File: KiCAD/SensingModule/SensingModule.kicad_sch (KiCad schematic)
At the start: 14 parts, among them J1 BUS, J2 MONITOR, U1 Arduino MKR WAN 1310

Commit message: 配線をつなげようとしたがうまくいかず　もう少し考えてみる
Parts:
- added H1, H2, H3, H4: MountingHole, MountingHole:MountingHole_4.3mm_M4, symbol Mechanical:MountingHole
- J1, J2: footprint Hirose_Connector:Hirose_DF11B-8DP-2DS -> TSRP_Connector:DF11-8DP-2DS
- U1: footprint ARDUINO_MKR_WAN_1310:BOARD_ARDUINO_MKR_WAN_1310 -> ARDUINO_MKR_WAN_1310 (1):BOARD_ARDUINO_MKR_WAN_1310

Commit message: MKRWAN問題解決
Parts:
- removed U1: Arduino MKR WAN 1310, ARDUINO_MKR_WAN_1310 (1):BOARD_ARDUINO_MKR_WAN_1310, symbol ABX00012:ABX00012
- added U1: ARDUINO_MKR_WAN_1310, TSRP_Arduino:BOARD_ARDUINO_MKR_WAN_1310, symbol ARDUINO_MKR_WAN_1310:ARDUINO_MKR_WAN_1310
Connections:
- net +3.3V: now also U1.J5_12 (+3V3)
- net +5V: now also U1.J5_13 (VIN)
- net CAN_RECEIVE_STATUS: now also U1.J3_9 (PA22/D0(PWM))
- net CAN_SEND_STATUS: now also U1.J3_10 (PA23/D1(PWM))
- net GND: now also U1.J5_11 (GND)
- net I2C_SCK: now also R8.1, U1.J5_7 (PA09/D12(PWM)/SCL(SC2)); no longer R7.1
- net I2C_SDA: now also R7.1, U1.J5_6 (PA08/D11/SDA(SC2)); no longer R8.1
- net LORA_RECEIVE_STATUS: now also U1.J3_13 (PB10/D4(PWM))
- net LORA_SEND_STATUS: now also U1.J3_14 (PB11/D5(PWM))
- net SPI_CS_FRAM0: now also U1.J3_3 (PB02/D16/AIN(10)/A1)
- net SPI_CS_FRAM1: now also U1.J3_4 (PB03/D17/AIN(11)/A2)
- net SPI_CS_FRAM2: now also U1.J3_11 (PA10/D2(PWM))
- net SPI_CS_FRAM3: now also U1.J3_12 (PA11/D3(PWM))
- net SPI_CS_MCP: now also U1.J5_2 (PA21/D7(PWM))
- net SPI_MISO: now also U1.J5_5 (PA19/D10(PWM)/CIPO(SC1))
- net SPI_MOSI: now also U1.J5_3 (PA16/D8(PWM)/COPI(SC1))
- net SPI_SCLK: now also U1.J5_4 (PA17/D9/SCK(SC1))
- net VREF_T1: now also U1.J3_5 (PA04/D18(PWM)/AIN(4)/A3)
- net VREF_T2: now also U1.J3_6 (PA05/D19(PWM)/AIN(5)/A4)
- net VREF_T3: now also U1.J3_7 (PA06/D20/AIN(6)/A5)
- net VREF_T4: now also U1.J3_8 (PA07/D21/AIN(7)/A6)
- net VREF_THERMISTOR: now also U1.J3_2 (PA02/D15/DAC0/AIN(0)/A0)
- no-connect marks 5 -> 6
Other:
- moved on the sheet: R3, R4, R5, R6, R7, R8, R9

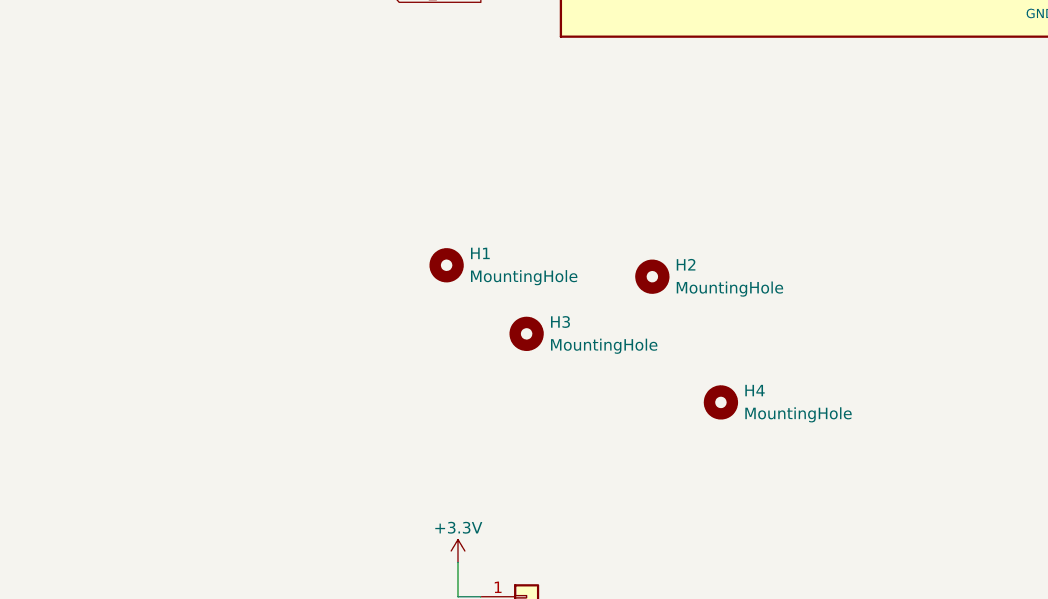
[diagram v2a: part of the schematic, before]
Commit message: 配線作業終了、確認お願いします
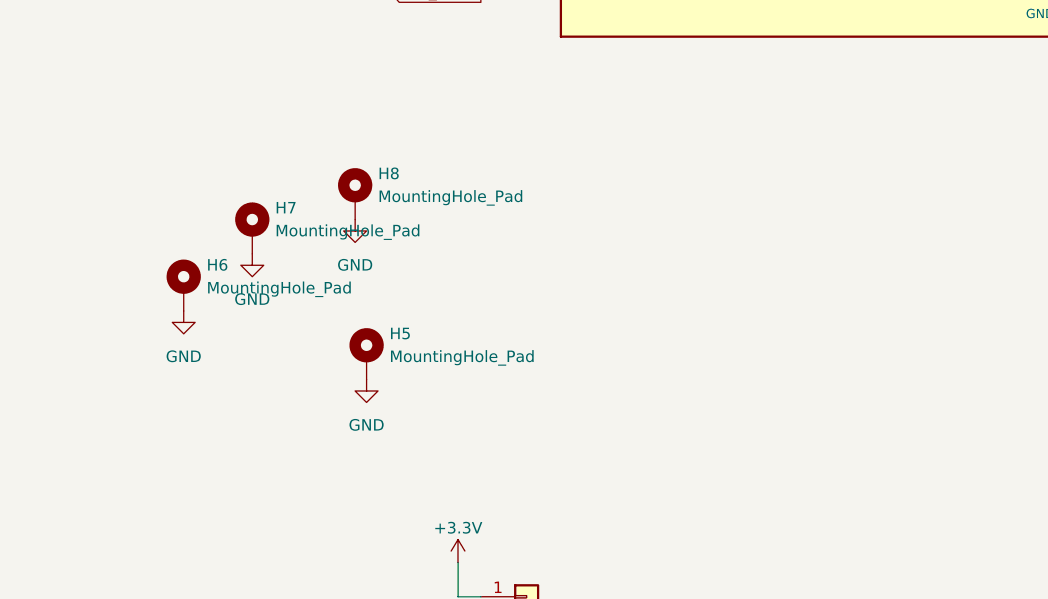
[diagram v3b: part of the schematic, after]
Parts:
- removed H1, H2, H3, H4: MountingHole, MountingHole:MountingHole_4.3mm_M4, symbol Mechanical:MountingHole
- added H5, H6, H7, H8: MountingHole_Pad, MountingHole:MountingHole_3.2mm_M3_DIN965_Pad_TopBottom, symbol Mechanical:MountingHole_Pad
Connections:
- net GND: now also H5.1, H6.1, H7.1, H8.1

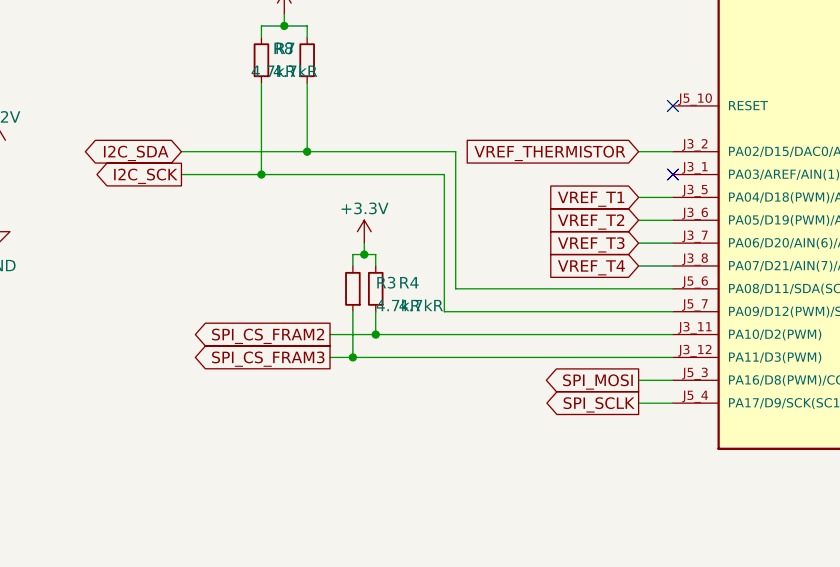
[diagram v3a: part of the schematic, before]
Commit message: Sensingの配線作業終わり、確認お願いします。
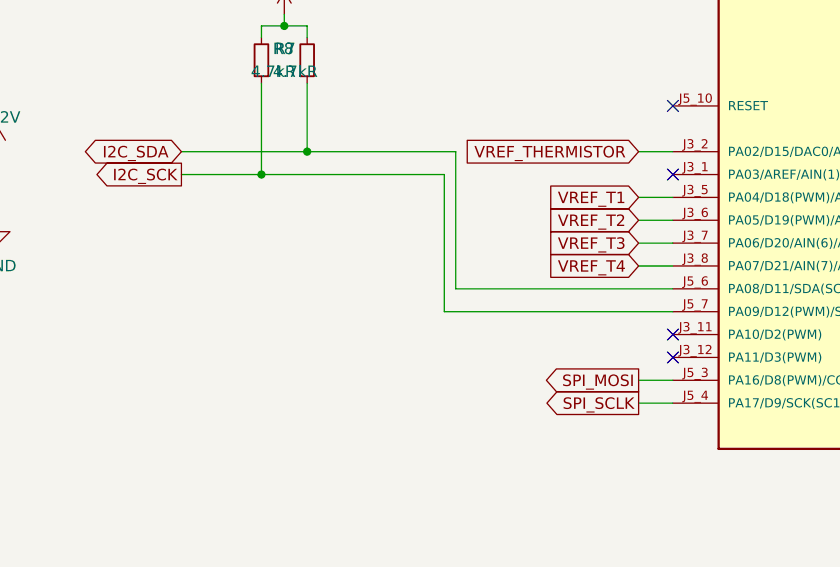
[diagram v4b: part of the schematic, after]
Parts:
- removed R3, R4: 4.7kR, Resistor_SMD:R_0603_1608Metric_Pad0.98x0.95mm_HandSolder, symbol Device:R_Small
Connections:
- net SPI_CS_FRAM2: no longer names the net of U1.J3_11 (PA10/D2(PWM))
- net SPI_CS_FRAM3: no longer names the net of U1.J3_12 (PA11/D3(PWM))
- no-connect marks 6 -> 8

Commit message: 配線確認お願いします
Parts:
- added R16: 4.7kR, Resistor_SMD:R_0603_1608Metric_Pad0.98x0.95mm_HandSolder, symbol Device:R_Small
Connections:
- net +3.3V: now also R16.2
- net SPI_CS_FRAM2: now reaches U1.J3_11 (PA10/D2(PWM))
- net SPI_CS_FRAM2: now also R16.1
- no-connect marks 8 -> 7
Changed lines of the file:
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@@
 	)
 	(junction
+		(at 102.87 73.66)
+		(diameter 0)
+		(color 0 0 0 0)
+	)
+	(junction
 		(at 255.27 53.34)
 		(diameter 0)
@@
 	)
 	(no_connect
-		(at 143.51 73.66)
-	)
-	(no_connect
 		(at 143.51 76.2)
 	)
@@
 	(wire
 		(pts
+			(xy 95.25 73.66) (xy 102.87 73.66)
+		)
+		(stroke
+			(width 0)
+			(type default)
+		)
+	)
+	(wire
+		(pts
 			(xy 63.5 130.81) (xy 63.5 133.35)
 		)
@@
 		)
 	)
+	(wire
+		(pts
+			(xy 102.87 69.85) (xy 102.87 73.66)
+		)
+		(stroke
+			(width 0)
+			(type default)
+		)
+	)
 	(bus
 		(pts
@@
 		)
 	)
+	(wire
+		(pts
+			(xy 102.87 73.66) (xy 143.51 73.66)
+		)
+		(stroke
+			(width 0)
+			(type default)
+		)
+	)
 	(label "GND"
 		(at 52.07 38.1 180)
@@
 		)
 	)
+	(global_label "SPI_CS_FRAM2"
+		(shape output)
+		(at 95.25 73.66 180)
+		(fields_autoplaced yes)
+		(effects
+			(font
+				(size 1.27 1.27)
+			)
+			(justify right)
+		)
+		(property "Intersheetrefs" "${INTERSHEET_REFS}"
+			(at 78.6577 73.66 0)
+			(effects
+				(font
+					(size 1.27 1.27)
+				)
+				(justify right)
+				(hide yes)
+			)
+		)
+	)
 	(global_label "VREF_THERMISTOR"
 		(shape input)
@@
 	)
 	(symbol
+		(lib_name "+3.3V_2")
+		(lib_id "power:+3.3V")
+		(at 102.87 64.77 0)
+		(unit 1)
+		(exclude_from_sim no)
+		(in_bom yes)
+		(on_board yes)
+		(dnp no)
+		(fields_autoplaced yes)
+		(property "Reference" "#PWR05"
+			(at 102.87 68.58 0)
+			(effects
+				(font
+					(size 1.27 1.27)
+				)
+				(hide yes)
+			)
+		)
+		(property "Value" "+3.3V"
+			(at 102.87 59.69 0)
+			(effects
+				(font
+					(size 1.27 1.27)
+				)
+			)
+		)
+		(property "Footprint" ""
+			(at 102.87 64.77 0)
+			(effects
+				(font
+					(size 1.27 1.27)
+				)
+				(hide yes)
+			)
+		)
+		(property "Datasheet" ""
+			(at 102.87 64.77 0)
+			(effects
+				(font
+					(size 1.27 1.27)
+				)
+				(hide yes)
+			)
+		)
+		(property "Description" "Power symbol creates a global label with name \"+3.3V\""
+			(at 102.87 64.77 0)
+			(effects
+				(font
+					(size 1.27 1.27)
+				)
+				(hide yes)
+			)
+		)
+		(pin "1"
+		)
+		(instances
+			(project ""
+				(path "/5f6205c9-e8e0-4a74-82d8-bdf647a68791"
+					(reference "#PWR05")
+					(unit 1)
+				)
+			)
+		)
+	)
+	(symbol
 		(lib_id "power:+3.3V")
 		(at 255.27 43.18 0)
@@
 					(unit 1)
 				)
+			)
+		)
+	)
+	(symbol
+		(lib_id "Device:R_Small")
+		(at 102.87 67.31 180)
+		(unit 1)
+		(exclude_from_sim no)
+		(in_bom yes)
+		(on_board yes)
+		(dnp no)
+		(property "Reference" "R16"
+			(at 104.14 66.04 0)
+			(effects
+				(font
+					(size 1.27 1.27)
+				)
+				(justify right)
+			)
+		)
+		(property "Value" "4.7kR"
+			(at 104.14 68.58 0)
+			(effects
+				(font
+					(size 1.27 1.27)
+				)
+				(justify right)
+			)
+		)
+		(property "Footprint" "Resistor_SMD:R_0603_1608Metric_Pad0.98x0.95mm_HandSolder"
+			(at 102.87 67.31 0)
+			(effects
+				(font
+					(size 1.27 1.27)
+				)
+				(hide yes)
+			)
+		)
+		(property "Datasheet" "https://www.chip1stop.com/view/dispDetail/DispDetail?partId=ROHM-0040161"
+			(at 102.87 67.31 0)
+			(effects
+				(font
+					(size 1.27 1.27)
+				)
+				(hide yes)
+			)
+		)
+		(property "Description" ""
+			(at 102.87 67.31 0)
+			(effects
+				(font
+					(size 1.27 1.27)
+				)
+				(hide yes)
+			)
+		)
+		(pin "1"
+		)
+		(pin "2"
+		)
+		(instances
+			(project "SensingModule"
+				(path "/5f6205c9-e8e0-4a74-82d8-bdf647a68791"
+					(reference "R16")
+					(unit 1)
+				)

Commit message: 簡単な警告を修正
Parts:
- J1, J2: footprint TSRP_Connector:DF11-8DP-2DS -> TSRP_Connector_Hirose:DF11-8DP-2DS
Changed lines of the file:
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@@
 			)
 		)
-		(property "Footprint" "TSRP_Connector:DF11-8DP-2DS"
+		(property "Footprint" "TSRP_Connector_Hirose:DF11-8DP-2DS"
 			(at 144.78 156.21 0)
 			(effects
@@
 			)
 		)
-		(property "Footprint" "TSRP_Connector:DF11-8DP-2DS"
+		(property "Footprint" "TSRP_Connector_Hirose:DF11-8DP-2DS"
 			(at 35.56 36.83 0)
 			(effects

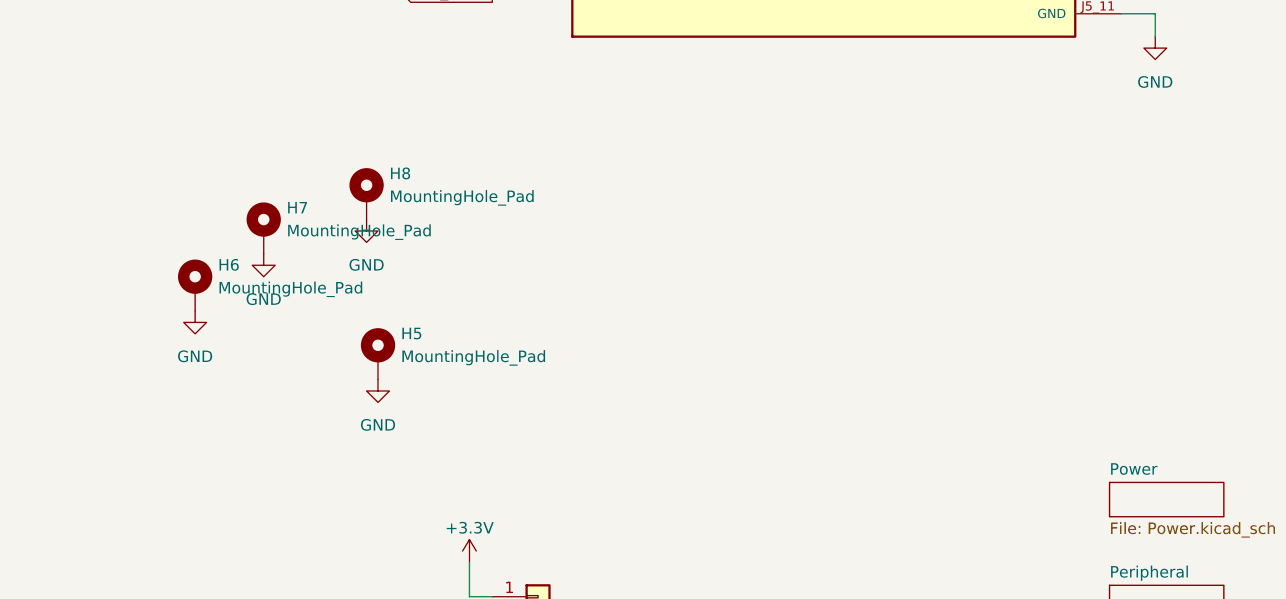
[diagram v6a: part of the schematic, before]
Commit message: BNO055のシンボルを変更．
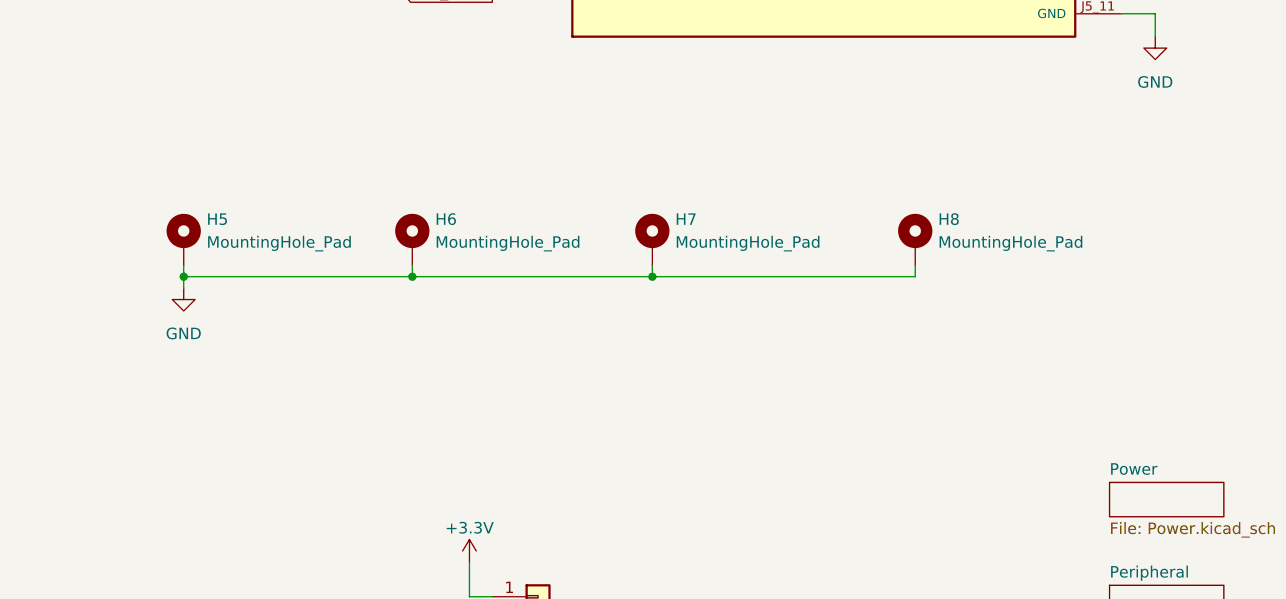
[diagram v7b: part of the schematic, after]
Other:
- moved on the sheet: H5, H6, H7, H8

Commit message: きれいに配線できるようになった．
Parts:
- removed R16: 4.7kR, Resistor_SMD:R_0603_1608Metric_Pad0.98x0.95mm_HandSolder, symbol Device:R_Small
- added R17: 4.7kR, Resistor_SMD:R_0603_1608Metric_Pad0.98x0.95mm_HandSolder, symbol Device:R_Small
- H5, H6, H7, H8: symbol Mechanical:MountingHole_Pad -> Mechanical:MountingHole; now in the parts list
- J2: now not fitted; now left out of the parts list
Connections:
- net +3.3V: now also R17.2; no longer R9.2
- net GND: no longer H5.1, H6.1, H7.1, H8.1
- net SPI_~{CS}_FeRAM2: now reaches U1.J5_8 (PB23/D13/RX(SC5))
- net SPI_~{CS}_FeRAM2: now also R17.1
- net SPI_~{CS}_FeRAM0: now reaches U1.J5_9 (PB22/D14/TX(SC5))
- net SPI_~{CS}_FeRAM0: now also R6.1
- net SPI_CS_FRAM0: no longer names the net of U1.J3_3 (PB02/D16/AIN(10)/A1)
- net SPI_CS_FRAM0: no longer R6.1
- net SPI_CS_FRAM1 renamed SPI_~{CS}_FeRAM1
- net SPI_CS_FRAM2: no longer names the net of U1.J3_11 (PA10/D2(PWM))
- new net +3.3VP: R9.2
- no-connect marks 7 -> 5
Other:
- moved on the sheet: R5, R6, R7, R8, R9
